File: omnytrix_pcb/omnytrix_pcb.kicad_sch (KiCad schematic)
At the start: 37 parts, among them J1 Conn_01x07, J2 Micro_SD_Card_Det2, J3 Conn_01x02, J4 USB_C_Receptacle_PowerOnly_6P, SW1 SW_Push, U1 LD3985M33R_SOT23, U2 TP4056, U3 STM32F411RCTx, U4 FS8205A, U5 DW01

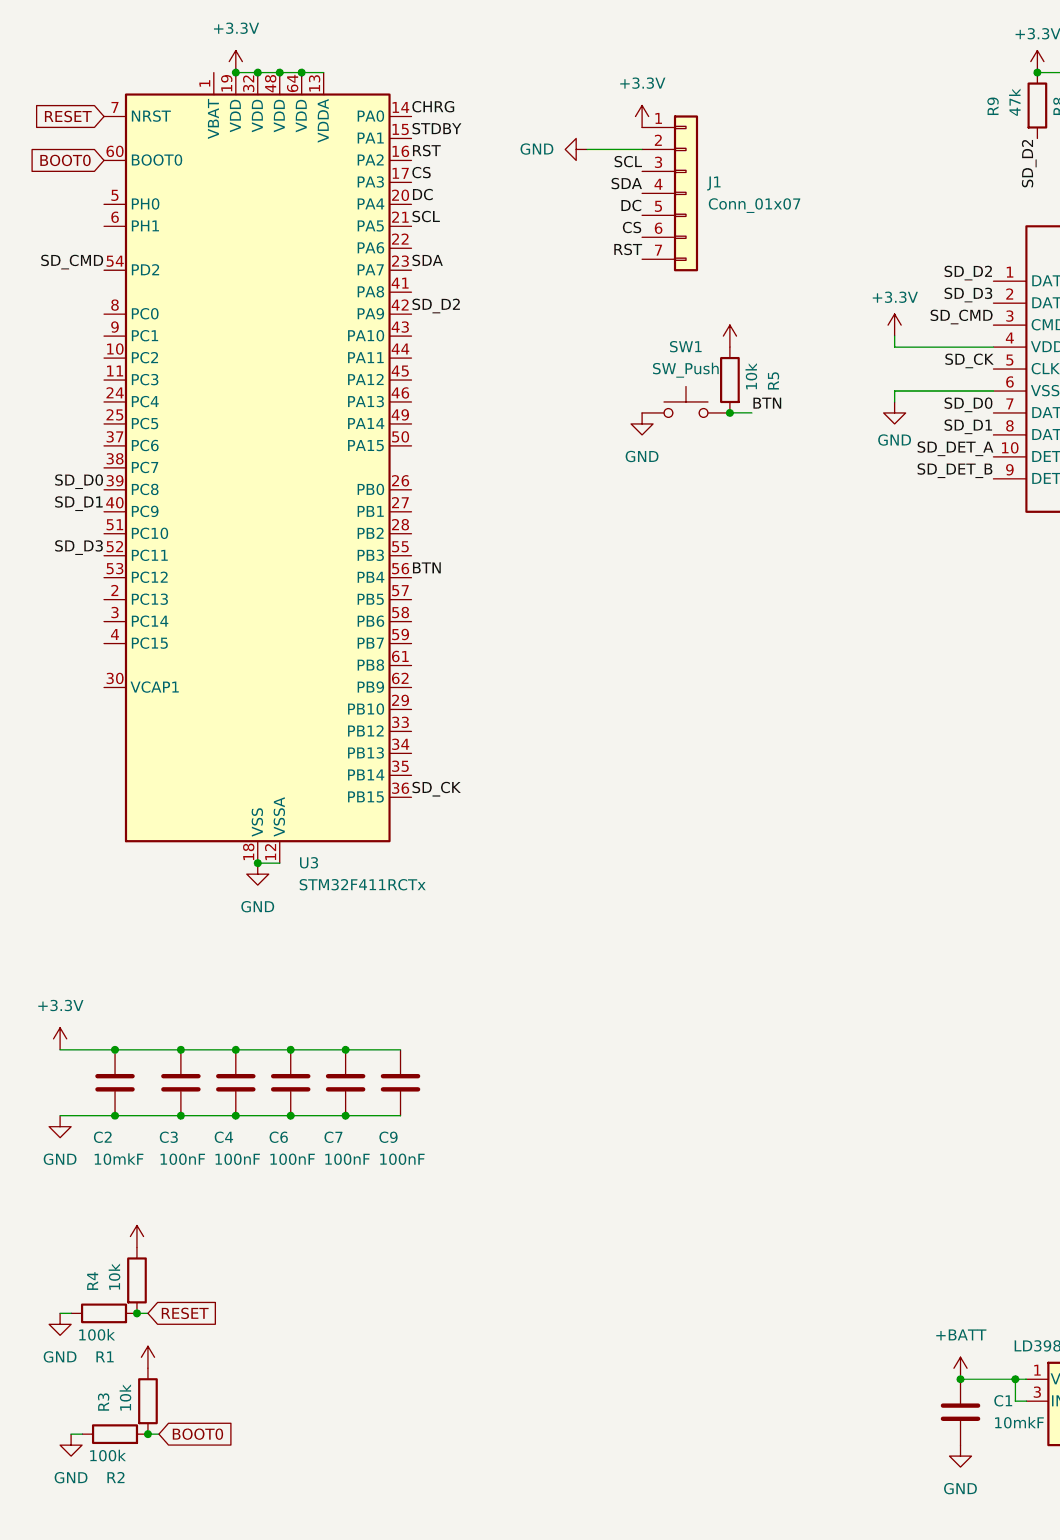
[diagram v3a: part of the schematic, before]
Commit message: add buzzer and encoder
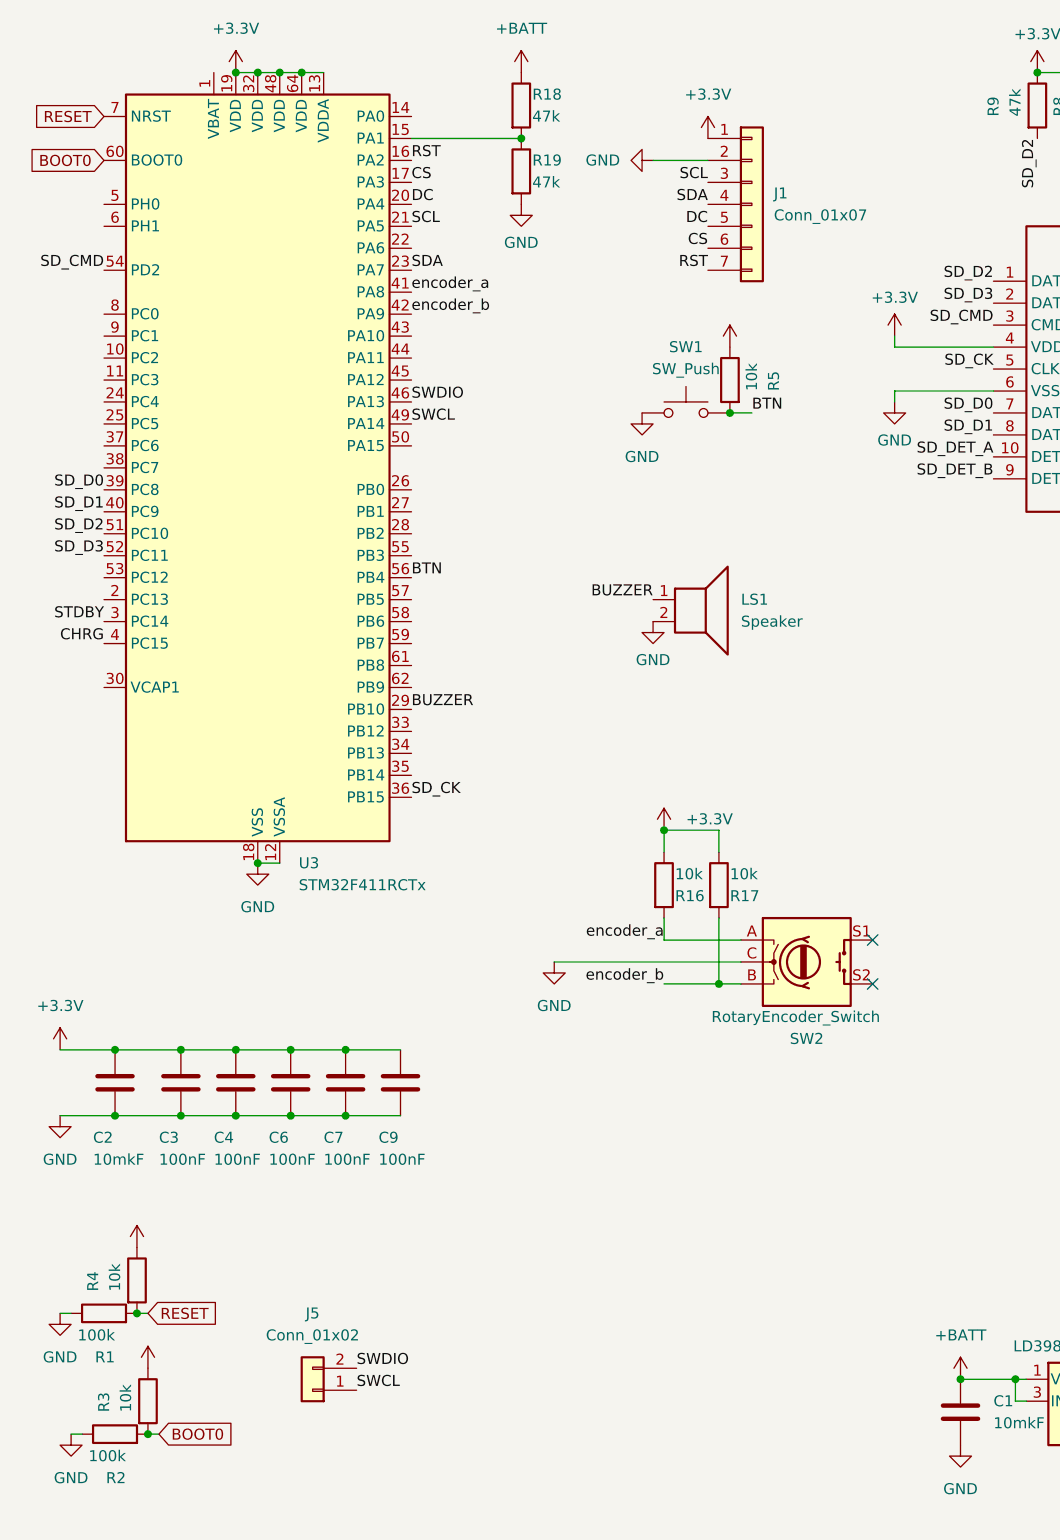
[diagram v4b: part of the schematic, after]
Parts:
- added J5: Conn_01x02, Connector_PinHeader_2.00mm:PinHeader_1x02_P2.00mm_Vertical, symbol Connector_Generic:Conn_01x02
- added LS1: Speaker, libs:smd_buzzer, symbol Device:Speaker
- added R16, R17: 10k, Resistor_SMD:R_0603_1608Metric_Pad0.98x0.95mm_HandSolder, symbol Device:R
- added R18, R19: 47k, Resistor_SMD:R_0603_1608Metric_Pad0.98x0.95mm_HandSolder, symbol Device:R
- added SW2: RotaryEncoder_Switch, libs:EC11_encoder, symbol Device:RotaryEncoder_Switch
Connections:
- net +3.3V: now also R16.1, R17.1
- net +BATT: now also R18.1
- net CHRG: now also U3.4 (PC15); no longer U3.14 (PA0)
- net GND: now also LS1.2, R19.2, SW2.C
- net SD_D2: now also U3.51 (PC10); no longer U3.42 (PA9)
- net STDBY: now also U3.3 (PC14); no longer U3.15 (PA1)
- net BUZZER: now reaches U3.29 (PB10)
- net BUZZER: now also LS1.1
- net encoder_a: now reaches U3.41 (PA8)
- net encoder_a: now also R16.2, SW2.A
- net SWDIO: now reaches U3.46 (PA13)
- net SWDIO: now also J5.2 (Pin_2)
- net SWCL: now reaches U3.49 (PA14)
- net SWCL: now also J5.1 (Pin_1)
- new net: R18.2, R19.1, U3.15 (PA1)
- new net encoder_b: R17.2, SW2.B, U3.42 (PA9)
- no-connect marks 6 -> 8
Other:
- moved on the sheet: J1

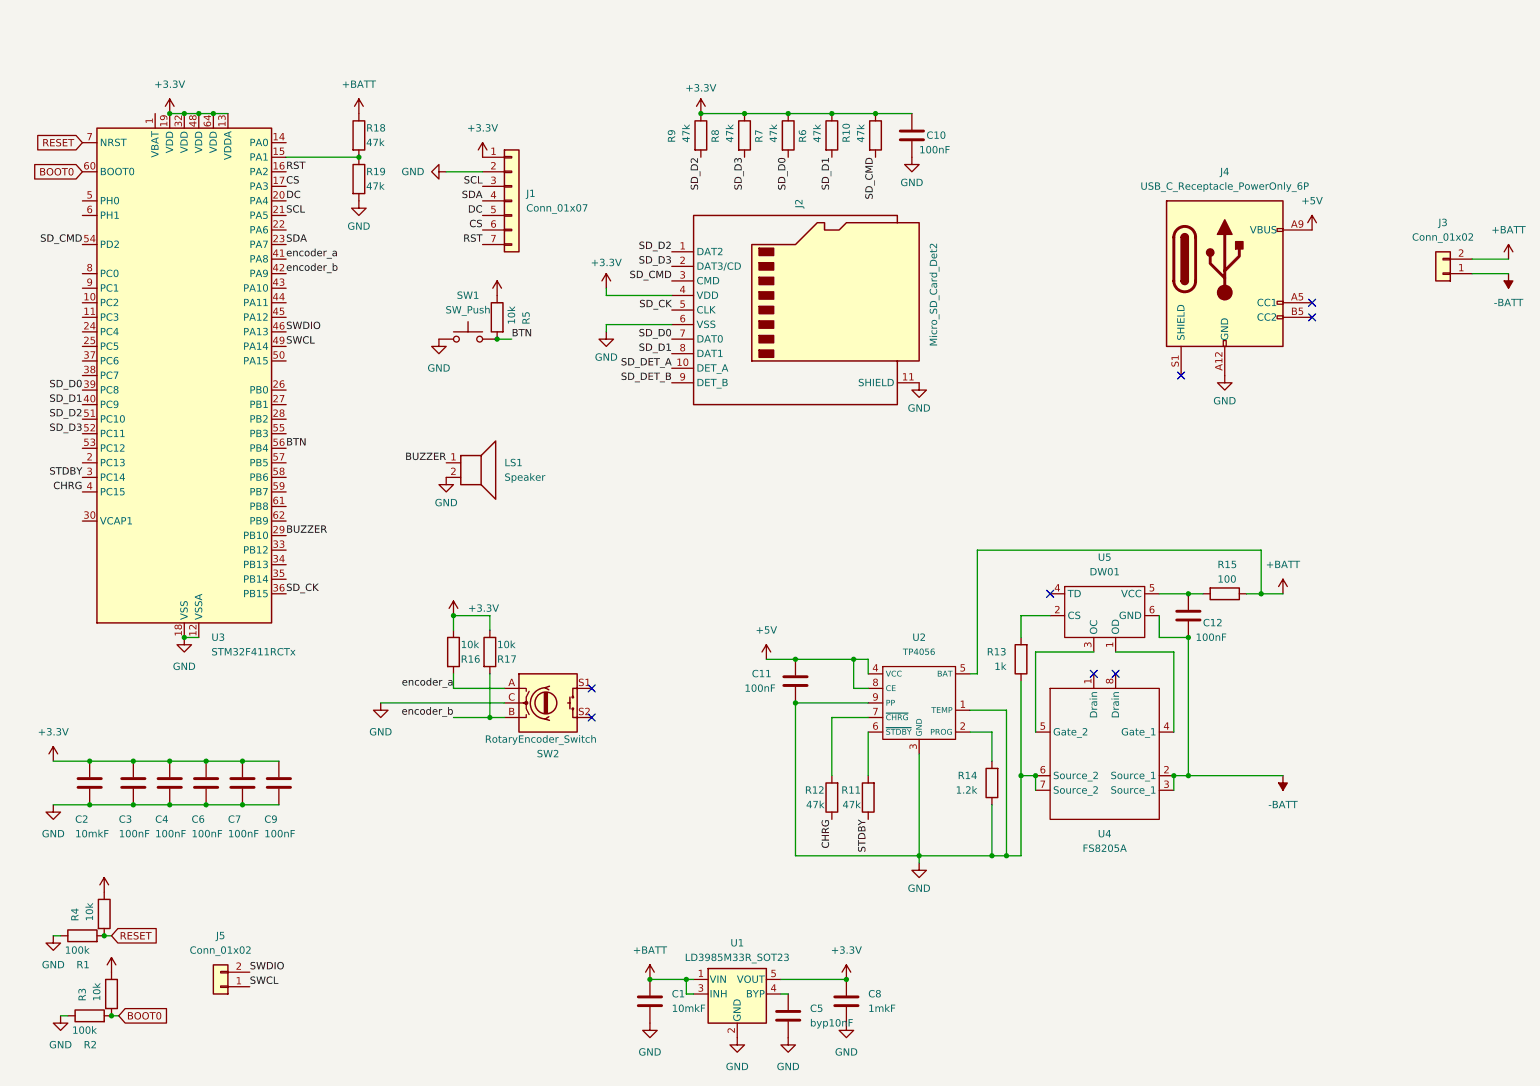
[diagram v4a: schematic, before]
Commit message: add vbat for rtc
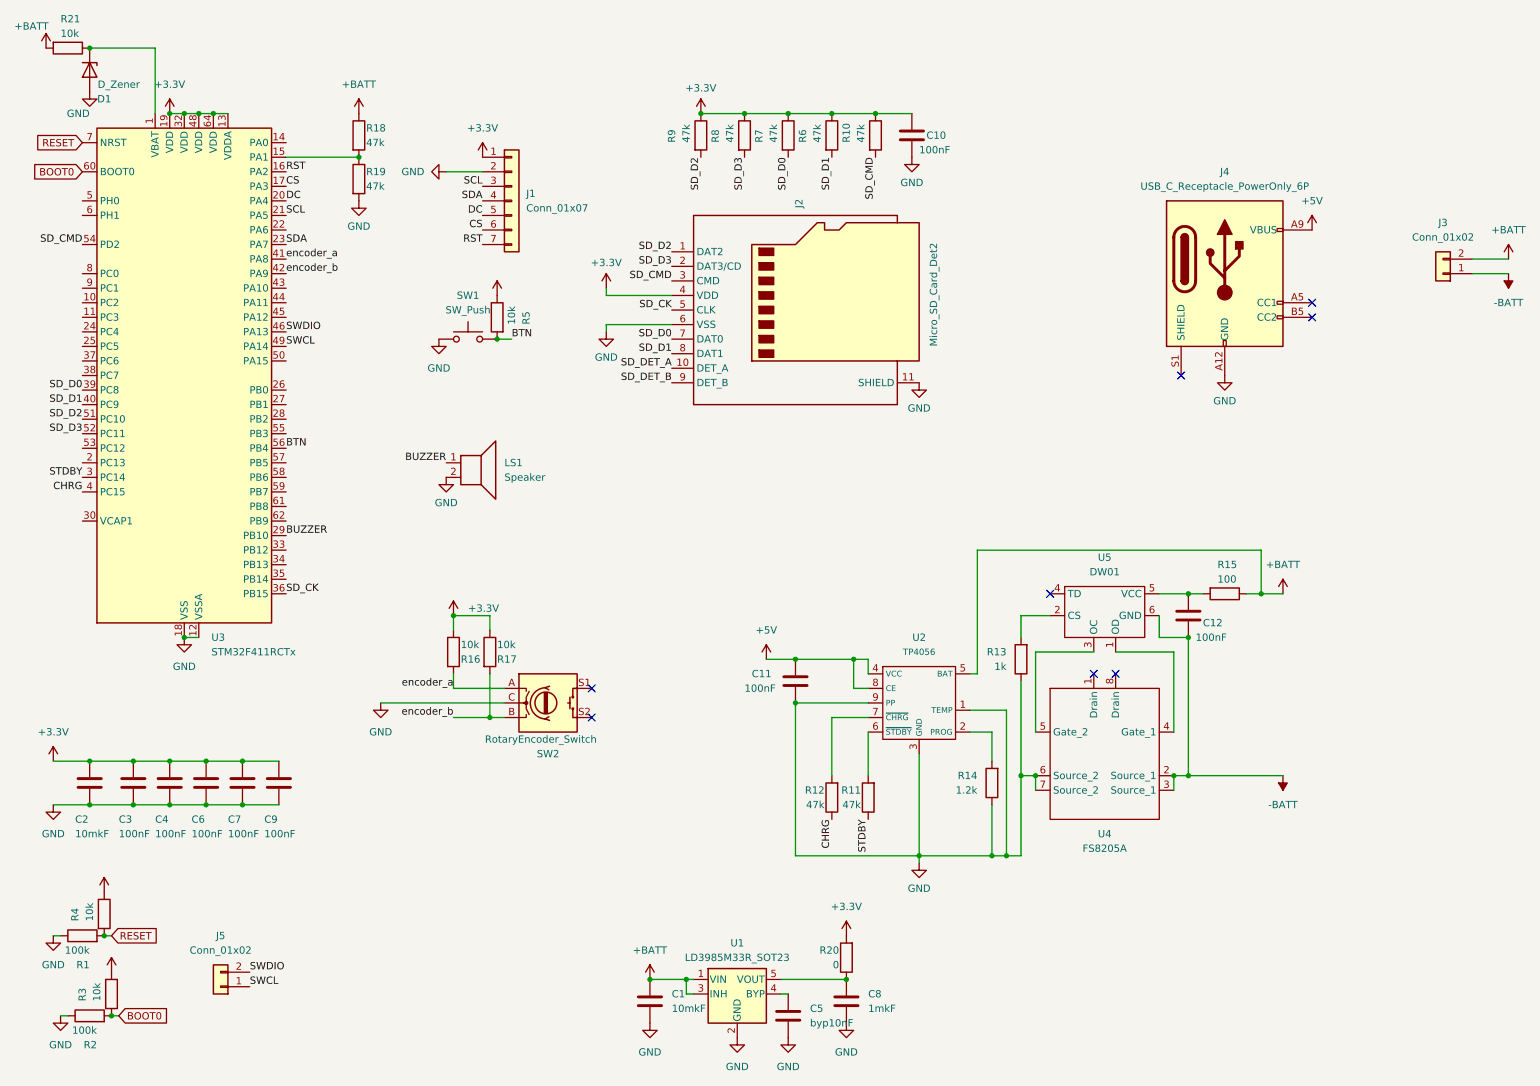
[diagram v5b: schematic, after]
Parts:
- added D1: D_Zener, Diode_SMD:D_SOD-323_HandSoldering, symbol Device:D_Zener
- added R20: 0, Resistor_SMD:R_0603_1608Metric_Pad0.98x0.95mm_HandSolder, symbol Device:R
- added R21: 10k, Resistor_SMD:R_0603_1608Metric_Pad0.98x0.95mm_HandSolder, symbol Device:R
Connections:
- net +3.3V: now also R20.2; no longer C8.1, U1.5 (VOUT)
- net +BATT: now also R21.2
- net GND: now also D1.2 (A)
- net at U3.1 (VBAT): now also D1.1 (K), R21.1
- new net: C8.1, R20.1, U1.5 (VOUT)
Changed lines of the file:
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@@
   (junction (at 31.75 180.34) (diameter 0) (color 0 0 0 0)
   )
+  (junction (at 27.94 11.43) (diameter 0) (color 0 0 0 0)
+  )
   (junction (at 134.62 22.86) (diameter 0) (color 0 0 0 0)
   )
@@
   (junction (at 132.08 173.99) (diameter 0) (color 0 0 0 0)
   )
+  (junction (at 125.73 173.99) (diameter 0) (color 0 0 0 0)
+  )
   (junction (at 160.02 173.99) (diameter 0) (color 0 0 0 0)
-  )
-  (junction (at 125.73 173.99) (diameter 0) (color 0 0 0 0)
   )
   (junction (at 49.53 22.86) (diameter 0) (color 0 0 0 0)
@@
     (stroke (width 0) (type default))
   )
+  (wire (pts (xy 27.94 11.43) (xy 39.37 11.43))
+    (stroke (width 0) (type default))
+  )
   (wire (pts (xy 193.04 116.84) (xy 193.04 130.81))
     (stroke (width 0) (type default))
@@
   )
   (wire (pts (xy 133.35 176.53) (xy 132.08 176.53))
+    (stroke (width 0) (type default))
+  )
+  (wire (pts (xy 39.37 11.43) (xy 39.37 22.86))
     (stroke (width 0) (type default))
   )
@@
     (property "Обозначения листов" "${INTERSHEET_REFS}" (at 41.5412 180.2606 0)
       (effects (font (size 1.27 1.27)) (justify left) hide)
+    )
+  )
+  (symbol (lib_id "power:GND") (at 27.94 19.05 0) (unit 1)
+    (in_bom yes) (on_board yes) (dnp no)
+    (property "Reference" "#PWR037" (at 27.94 25.4 0)
+      (effects (font (size 1.27 1.27)) hide)
+    )
+    (property "Value" "GND" (at 27.94 22.86 0)
+      (effects (font (size 1.27 1.27)) (justify right))
+    )
+    (property "Footprint" "" (at 27.94 19.05 0)
+      (effects (font (size 1.27 1.27)) hide)
+    )
+    (property "Datasheet" "" (at 27.94 19.05 0)
+      (effects (font (size 1.27 1.27)) hide)
+    )
+    (pin "1")
+    (instances
+      (project "omnytrix_pcb"
+        (path "/e3ad1182-7354-43c6-b92c-8e5464d9863f"
+          (reference "#PWR037") (unit 1)
+        )
+      )
+      (project "Surface_keyboard"
+        (path "/ff9b0ae9-6a6c-41a5-a3d6-72dd8cdc1d99"
+          (reference "#PWR0103") (unit 1)
+        )
+      )
     )
   )
@@
     )
   )
+  (symbol (lib_id "power:+BATT") (at 20.32 11.43 0) (unit 1)
+    (in_bom yes) (on_board yes) (dnp no)
+    (property "Reference" "#PWR038" (at 20.32 15.24 0)
+      (effects (font (size 1.27 1.27)) hide)
+    )
+    (property "Value" "+BATT" (at 17.78 7.62 0)
+      (effects (font (size 1.27 1.27)))
+    )
+    (property "Footprint" "" (at 20.32 11.43 0)
+      (effects (font (size 1.27 1.27)) hide)
+    )
+    (property "Datasheet" "" (at 20.32 11.43 0)
+      (effects (font (size 1.27 1.27)) hide)
+    )
+    (pin "1")
+    (instances
+      (project "omnytrix_pcb"
+        (path "/e3ad1182-7354-43c6-b92c-8e5464d9863f"
+          (reference "#PWR038") (unit 1)
+        )
+      )
+    )
+  )
   (symbol (lib_id "Device:R") (at 97.79 116.84 0) (unit 1)
     (in_bom yes) (on_board yes) (dnp no)
@@
     )
   )
-  (symbol (lib_id "power:+3.3V") (at 160.02 173.99 0) (unit 1)
-    (in_bom yes) (on_board yes) (dnp no) (fields_autoplaced)
-    (property "Reference" "#PWR09" (at 160.02 177.8 0)
-      (effects (font (size 1.27 1.27)) hide)
-    )
-    (property "Value" "+3.3V" (at 160.02 168.91 0)
-      (effects (font (size 1.27 1.27)))
-    )
-    (property "Footprint" "" (at 160.02 173.99 0)
-      (effects (font (size 1.27 1.27)) hide)
-    )
-    (property "Datasheet" "" (at 160.02 173.99 0)
+  (symbol (lib_id "Device:R") (at 24.13 11.43 270) (unit 1)
+    (in_bom yes) (on_board yes) (dnp no)
+    (property "Reference" "R21" (at 22.86 6.35 90)
+      (effects (font (size 1.27 1.27)) (justify left))
+    )
+    (property "Value" "10k" (at 22.86 8.89 90)
+      (effects (font (size 1.27 1.27)) (justify left))
+    )
+    (property "Footprint" "Resistor_SMD:R_0603_1608Metric_Pad0.98x0.95mm_HandSolder" (at 24.13 9.652 90)
+      (effects (font (size 1.27 1.27)) hide)
+    )
+    (property "Datasheet" "~" (at 24.13 11.43 0)
+      (effects (font (size 1.27 1.27)) hide)
+    )
+    (pin "1")
+    (pin "2")
+    (instances
+      (project "omnytrix_pcb"
+        (path "/e3ad1182-7354-43c6-b92c-8e5464d9863f"
+          (reference "R21") (unit 1)
+        )
+      )
+      (project "Surface_keyboard"
+        (path "/ff9b0ae9-6a6c-41a5-a3d6-72dd8cdc1d99"
+          (reference "R1") (unit 1)
+        )
+      )
+    )
+  )
+  (symbol (lib_id "power:+3.3V") (at 160.02 166.37 0) (unit 1)
+    (in_bom yes) (on_board yes) (dnp no) (fields_autoplaced)
+    (property "Reference" "#PWR09" (at 160.02 170.18 0)
+      (effects (font (size 1.27 1.27)) hide)
+    )
+    (property "Value" "+3.3V" (at 160.02 161.29 0)
+      (effects (font (size 1.27 1.27)))
+    )
+    (property "Footprint" "" (at 160.02 166.37 0)
+      (effects (font (size 1.27 1.27)) hide)
+    )
+    (property "Datasheet" "" (at 160.02 166.37 0)
       (effects (font (size 1.27 1.27)) hide)
     )
@@
         (path "/ff9b0ae9-6a6c-41a5-a3d6-72dd8cdc1d99"
           (reference "#PWR0112") (unit 1)
+        )
+      )
+    )
+  )
+  (symbol (lib_id "Device:D_Zener") (at 27.94 15.24 270) (unit 1)
+    (in_bom yes) (on_board yes) (dnp no)
+    (property "Reference" "D1" (at 30.48 20.32 90)
+      (effects (font (size 1.27 1.27)))
+    )
+    (property "Value" "D_Zener" (at 33.02 17.78 90)
+      (effects (font (size 1.27 1.27)))
+    )
+    (property "Footprint" "Diode_SMD:D_SOD-323_HandSoldering" (at 27.94 15.24 0)
+      (effects (font (size 1.27 1.27)) hide)
+    )
+    (property "Datasheet" "~" (at 27.94 15.24 0)
+      (effects (font (size 1.27 1.27)) hide)
+    )
+    (pin "1")
+    (pin "2")
+    (instances
+      (project "omnytrix_pcb"
+        (path "/e3ad1182-7354-43c6-b92c-8e5464d9863f"
+          (reference "D1") (unit 1)
         )
       )
@@
         )
       )
+    )
+  )
+  (symbol (lib_id "Device:R") (at 160.02 170.18 180) (unit 1)
+    (in_bom yes) (on_board yes) (dnp no)
+    (property "Reference" "R20" (at 158.75 168.91 0)
+      (effects (font (size 1.27 1.27)) (justify left))
+    )
+    (property "Value" "0" (at 158.75 171.45 0)
+      (effects (font (size 1.27 1.27)) (justify left))
+    )
+    (property "Footprint" "Resistor_SMD:R_0603_1608Metric_Pad0.98x0.95mm_HandSolder" (at 161.798 170.18 90)
+      (effects (font (size 1.27 1.27)) hide)
+    )
+    (property "Datasheet" "~" (at 160.02 170.18 0)
+      (effects (font (size 1.27 1.27)) hide)
+    )
+    (pin "1")
+    (pin "2")
+    (instances
+      (project "omnytrix_pcb"
+        (path "/e3ad1182-7354-43c6-b92c-8e5464d9863f"
+          (reference "R20") (unit 1)
+        )
+      )
+      (project "Surface_keyboard"
+        (path "/ff9b0ae9-6a6c-41a5-a3d6-72dd8cdc1d99"
+          (reference "R1") (unit 1)
+        )
+      )
